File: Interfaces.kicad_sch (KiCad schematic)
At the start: 14 parts, among them J5 SWD1, J6 I2C1_Headers, J8 UART1_HDR

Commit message: Update
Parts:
- removed J5: SWD1, Connector_PinHeader_2.54mm:PinHeader_2x04_P2.54mm_Horizontal, symbol Connector_Generic:Conn_02x04_Odd_Even
- removed J8: UART1_HDR, Connector_PinHeader_2.54mm:PinHeader_2x03_P2.54mm_Horizontal, symbol Connector_Generic:Conn_02x03_Odd_Even
- removed R44: 33R, Resistor_SMD:R_0805_2012Metric, symbol Device:R
- added J1: I/O_HDR, Connector_PinHeader_2.54mm:PinHeader_2x04_P2.54mm_Horizontal, symbol Connector_Generic:Conn_02x04_Odd_Even
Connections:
- net GND: now also J1.1 (Pin_1), J1.3 (Pin_3), J1.5 (Pin_5), J1.7 (Pin_7)
- new net I/O_HDR0: J1.2 (Pin_2)
- new net I/O_HDR1: J1.4 (Pin_4)
- new net I/O_HDR2: J1.6 (Pin_6)
- new net I/O_HDR3: J1.8 (Pin_8)
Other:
- note removed: "ST-LINK Connections: VCP_TX, SWCLK, SWDIO, VCP_RX, NRST"
- moved on the sheet: C30, DI4, H1, H2, H3, H4, J6, R24, R26, R27, U6

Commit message: Update
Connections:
- net +3.3V: now also J1.1 (Pin_1)
- net GND: no longer J1.1 (Pin_1)
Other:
- company: (none) -> Peter Hancak
- title: (none) -> USB-PD Board
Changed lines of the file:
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@@
 	(generator_version "8.0")
 	(paper "USLetter")
+	(title_block
+		(title "USB-PD Board")
+		(date "2025-12-03")
+		(rev "B")
+		(company "Peter Hancak")
+	)
 	(junction
 		(at 97.79 160.02)
@@
 	)
 	(junction
-		(at 186.69 64.77)
-		(diameter 0)
-		(color 0 0 0 0)
-	)
-	(junction
 		(at 100.33 177.8)
 		(diameter 0)
@@
 	(wire
 		(pts
+			(xy 186.69 62.23) (xy 186.69 60.96)
+		)
+		(stroke
+			(width 0)
+			(type default)
+		)
+	)
+	(wire
+		(pts
 			(xy 209.55 146.05) (xy 200.66 146.05)
 		)
@@
 	(wire
 		(pts
+			(xy 52.07 67.31) (xy 78.74 67.31)
+		)
+		(stroke
+			(width 0)
+			(type default)
+		)
+	)
+	(wire
+		(pts
+			(xy 93.98 168.91) (xy 91.44 168.91)
+		)
+		(stroke
+			(width 0)
+			(type default)
+		)
+	)
+	(wire
+		(pts
+			(xy 78.74 67.31) (xy 118.11 67.31)
+		)
+		(stroke
+			(width 0)
+			(type default)
+		)
+	)
+	(wire
+		(pts
+			(xy 99.06 83.82) (xy 91.44 83.82)
+		)
+		(stroke
+			(width 0)
+			(type default)
+		)
+	)
+	(wire
+		(pts
 			(xy 194.31 62.23) (xy 186.69 62.23)
 		)
@@
 	(wire
 		(pts
-			(xy 52.07 67.31) (xy 78.74 67.31)
-		)
-		(stroke
-			(width 0)
-			(type default)
-		)
-	)
-	(wire
-		(pts
-			(xy 93.98 168.91) (xy 91.44 168.91)
-		)
-		(stroke
-			(width 0)
-			(type default)
-		)
-	)
-	(wire
-		(pts
-			(xy 78.74 67.31) (xy 118.11 67.31)
-		)
-		(stroke
-			(width 0)
-			(type default)
-		)
-	)
-	(wire
-		(pts
-			(xy 99.06 83.82) (xy 91.44 83.82)
-		)
-		(stroke
-			(width 0)
-			(type default)
-		)
-	)
-	(wire
-		(pts
 			(xy 135.89 62.23) (xy 138.43 62.23)
 		)
@@
 		(pts
 			(xy 200.66 144.78) (xy 200.66 146.05)
-		)
-		(stroke
-			(width 0)
-			(type default)
-		)
-	)
-	(wire
-		(pts
-			(xy 186.69 62.23) (xy 186.69 64.77)
 		)
 		(stroke
@@
 					(unit 1)
 				)
+			)
+		)
+	)
+	(symbol
+		(lib_id "power:+3.3V")
+		(at 186.69 60.96 0)
+		(mirror y)
+		(unit 1)
+		(exclude_from_sim no)
+		(in_bom yes)
+		(on_board yes)
+		(dnp no)
+		(property "Reference" "#PWR019"
+			(at 186.69 64.77 0)
+			(effects
+				(font
+					(size 1.27 1.27)
+				)
+				(hide yes)
+			)
+		)
+		(property "Value" "+3.3V"
+			(at 184.658 57.912 90)
+			(effects
+				(font
+					(size 1.27 1.27)
+				)
+				(justify right)
+			)
+		)
+		(property "Footprint" ""
+			(at 186.69 60.96 0)
+			(effects
+				(font
+					(size 1.27 1.27)
+				)
+				(hide yes)
+			)
+		)
+		(property "Datasheet" ""
+			(at 186.69 60.96 0)
+			(effects
+				(font
+					(size 1.27 1.27)
+				)
+				(hide yes)
+			)
+		)
+		(property "Description" "Power symbol creates a global label with name \"+3.3V\""
+			(at 186.69 60.96 0)
+			(effects
+				(font
+					(size 1.27 1.27)
+				)
+				(hide yes)
+			)
+		)
+		(pin "1"
+		)
+		(instances
+			(project "USBPD_Board"
+				(path "/b3855754-13ea-49fc-935d-9d42ea1a9383/7fc71731-05e0-47b0-9baf-64dcc51f2872"
+					(reference "#PWR019")
+					(unit 1)
+				)

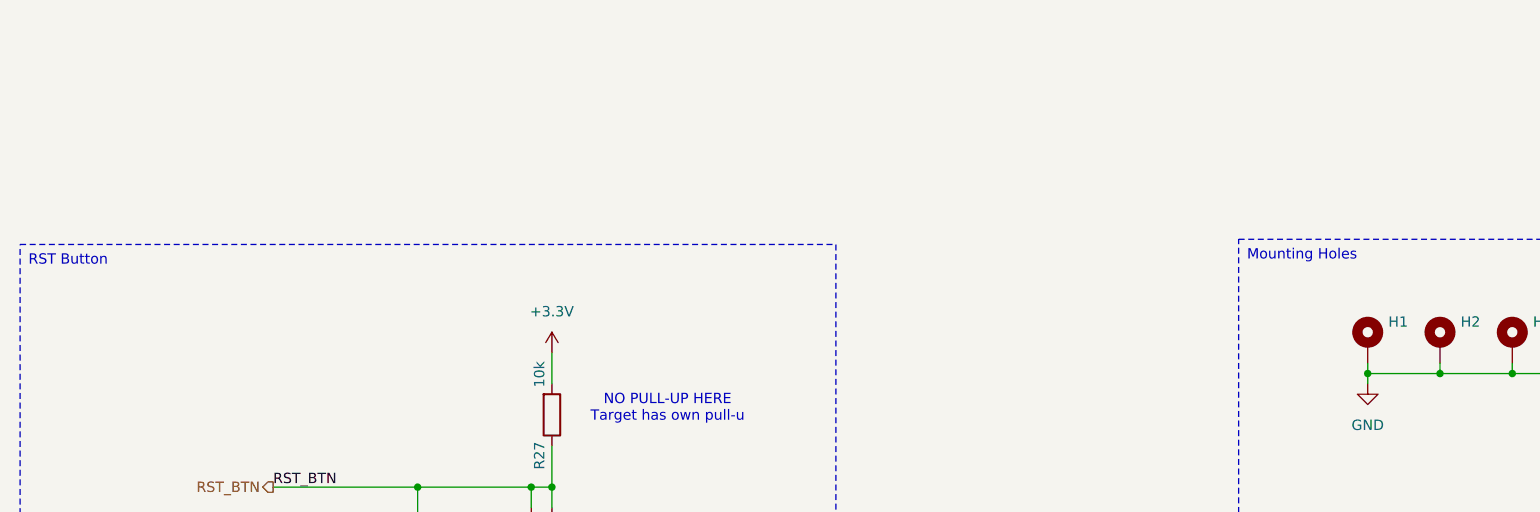
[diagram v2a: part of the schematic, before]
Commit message: Change Kicad version
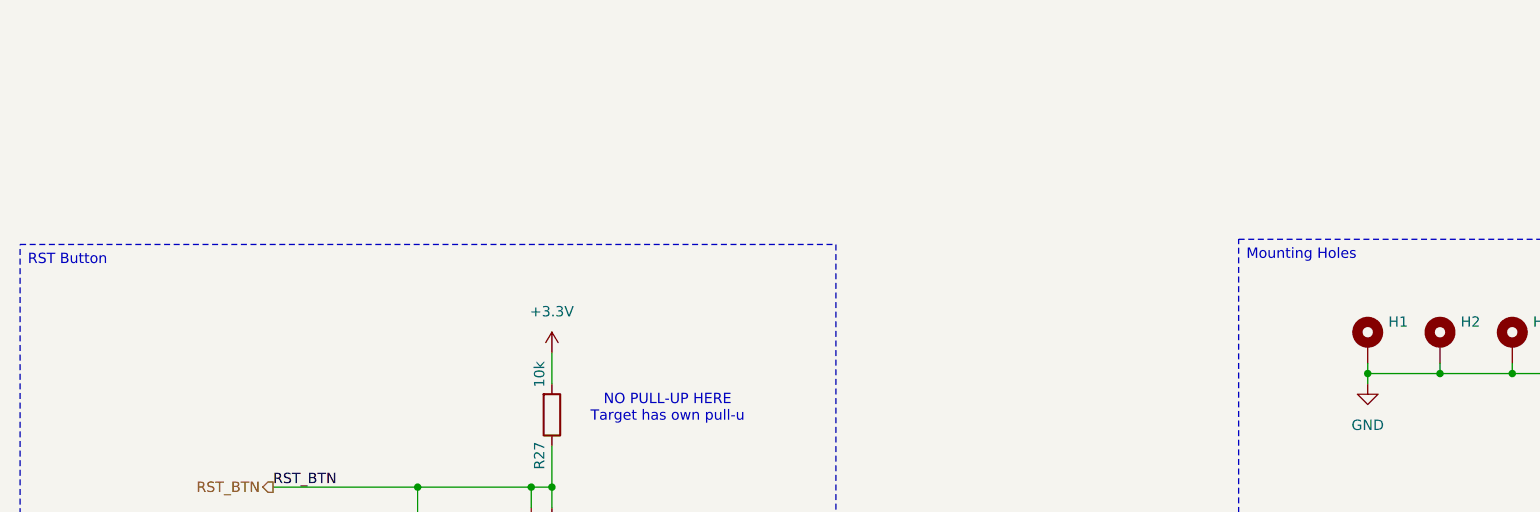
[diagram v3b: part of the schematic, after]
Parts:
- U6: value ~ -> (none)
